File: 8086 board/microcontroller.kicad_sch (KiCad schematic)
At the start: 7 parts, among them U10 74HC595, U11 74HC595, U12 74HC595, U13 74HC165, U14 74HC165, U2 ATmega328P-A, U25 CP2102N-Axx-xQFN28

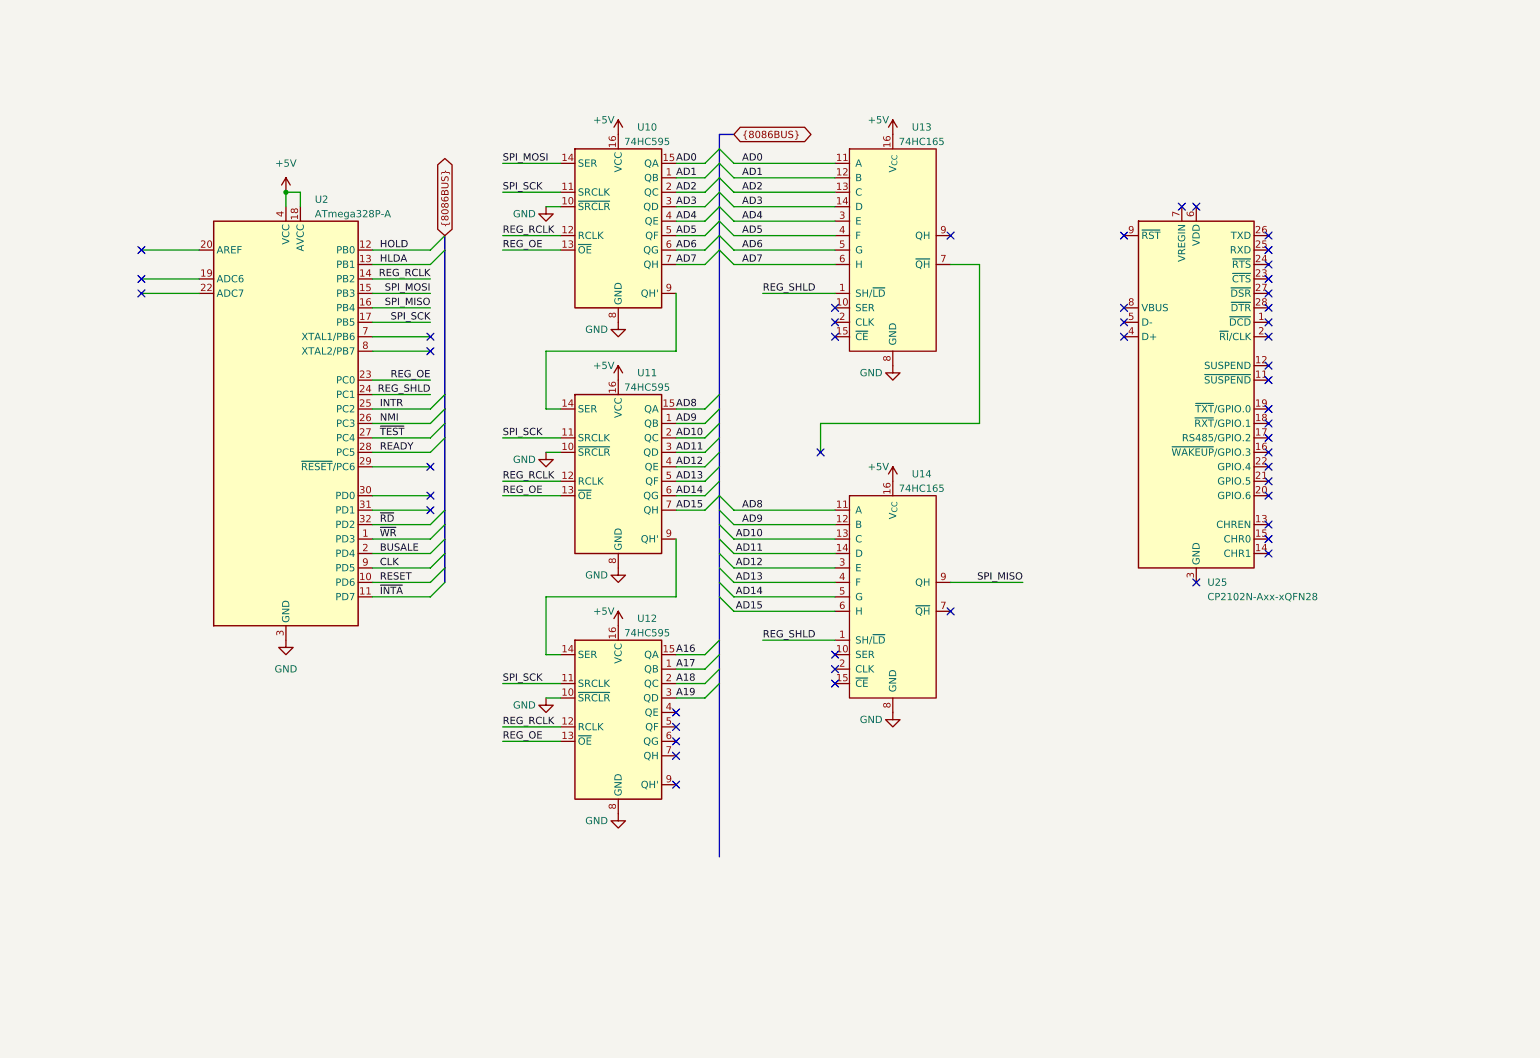
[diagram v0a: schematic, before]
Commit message: refactoring schematic files and structure
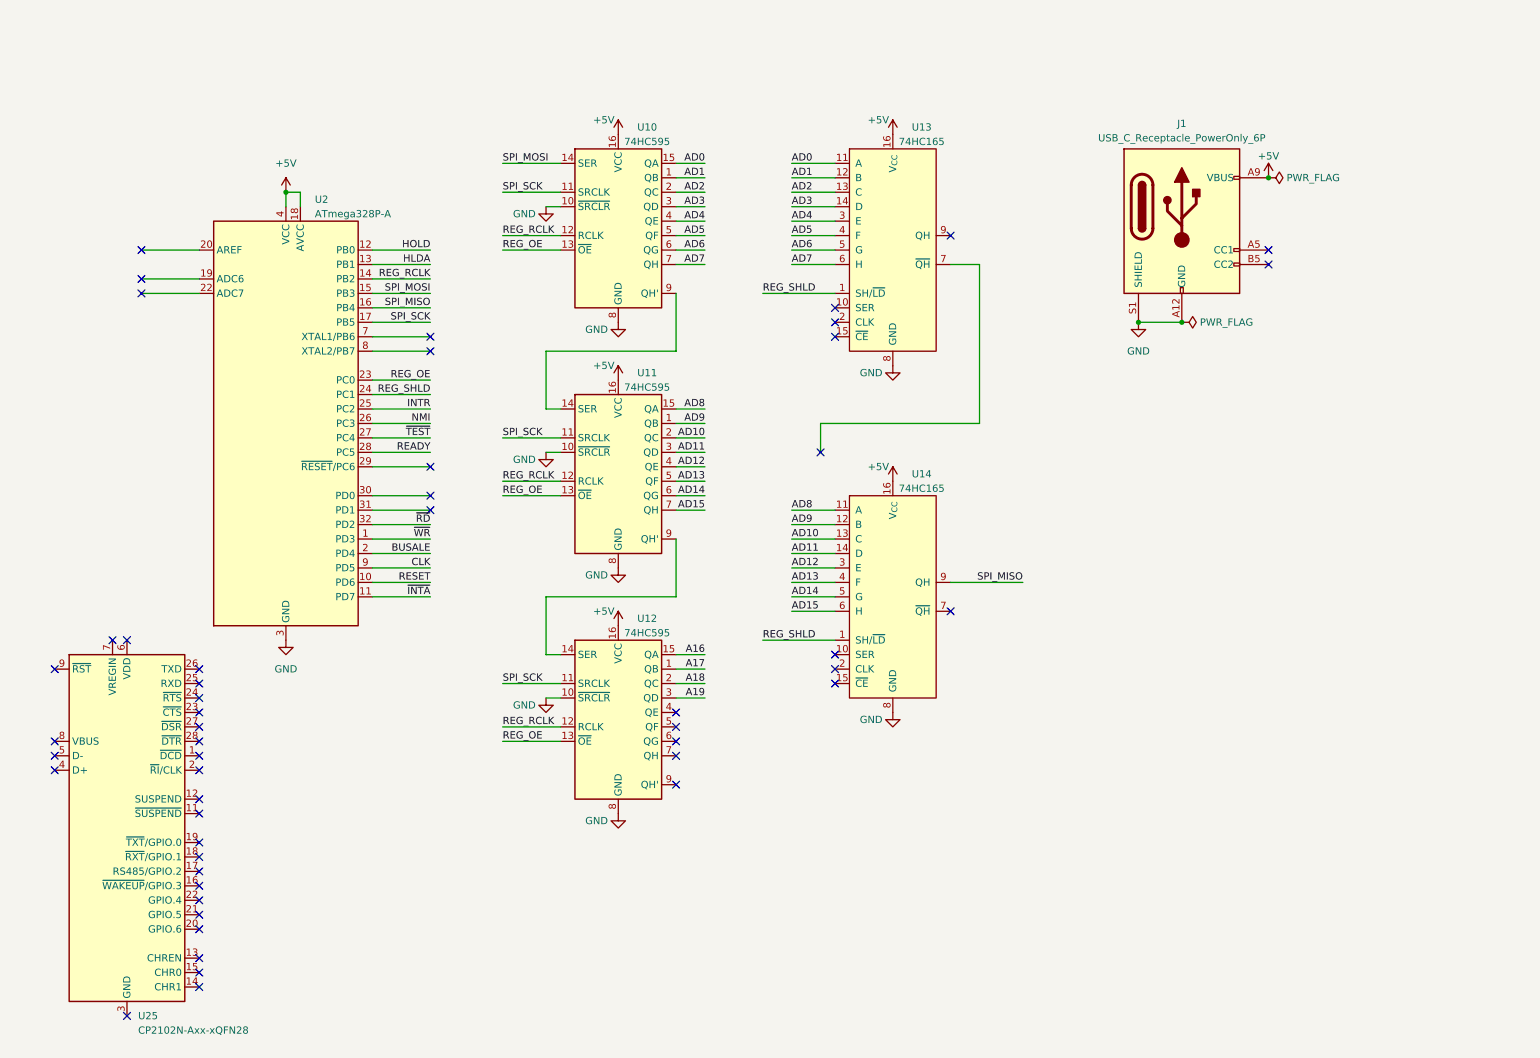
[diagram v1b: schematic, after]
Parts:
- added J1: USB_C_Receptacle_PowerOnly_6P, symbol Connector:USB_C_Receptacle_PowerOnly_6P
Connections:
- net +5V: now also J1.A9 (VBUS), J1.B9 (VBUS)
- net GND: now also J1.A12 (GND), J1.B12 (GND), J1.S1 (SHIELD)
- no-connect marks 49 -> 51
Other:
- moved on the sheet: U25

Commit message: better schematic. initial pcb layout
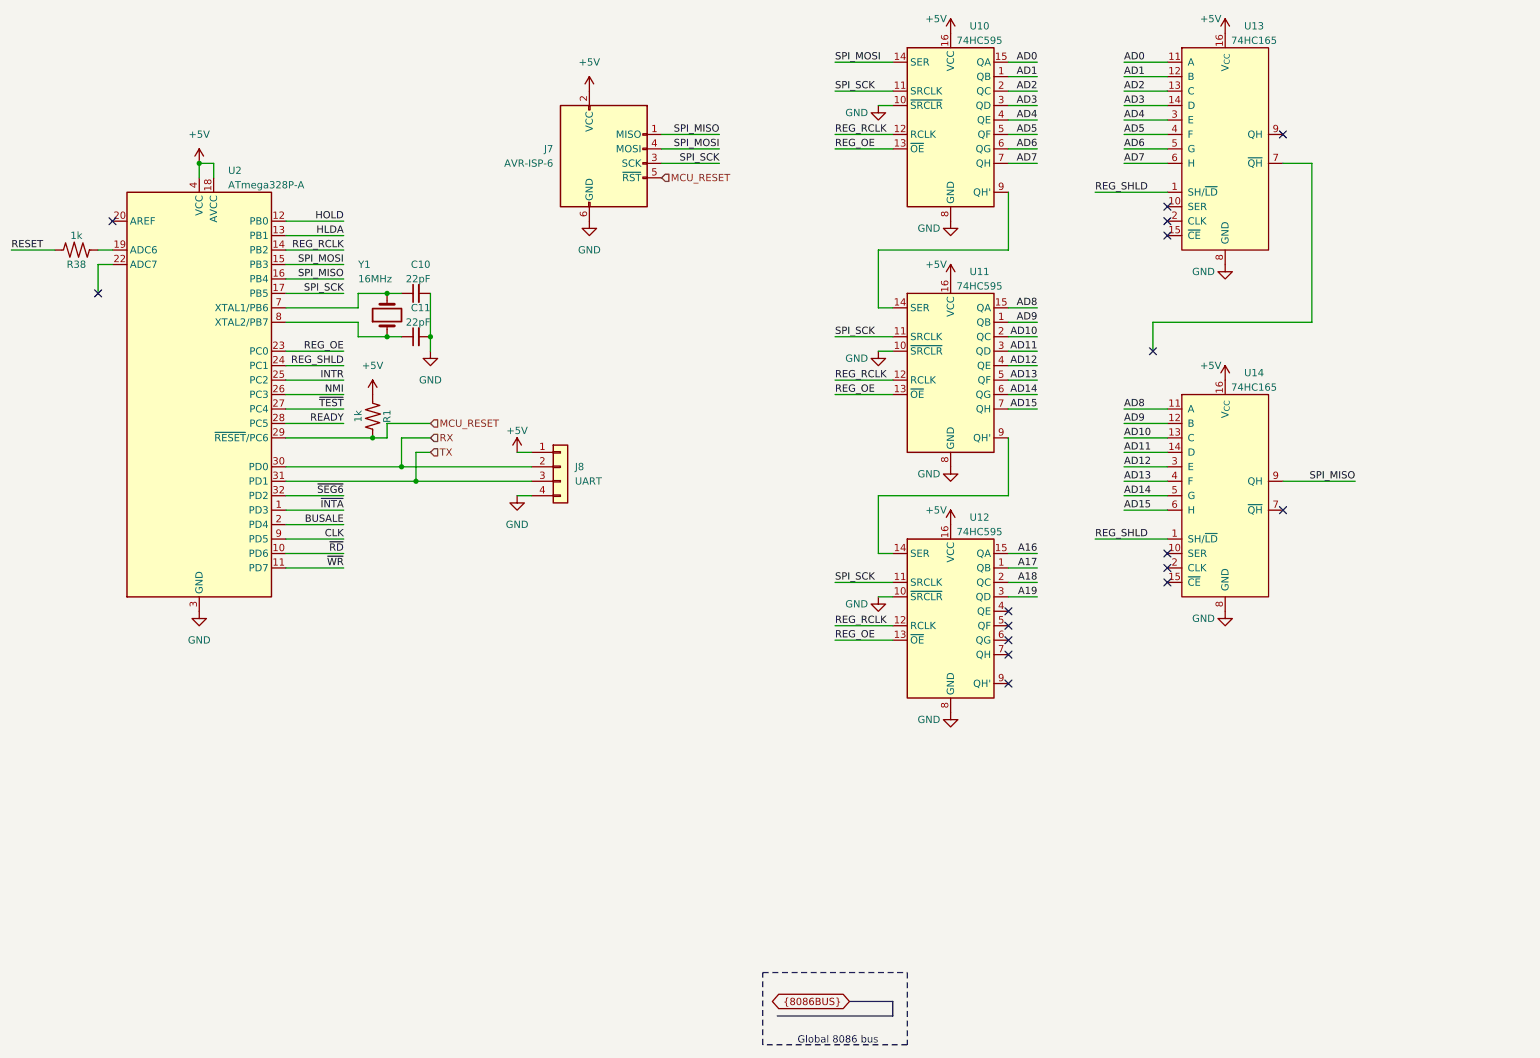
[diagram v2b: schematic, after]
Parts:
- removed J1: USB_C_Receptacle_PowerOnly_6P, symbol Connector:USB_C_Receptacle_PowerOnly_6P
- removed U25: CP2102N-Axx-xQFN28, Package_DFN_QFN:QFN-28-1EP_5x5mm_P0.5mm_EP3.35x3.35mm, symbol Interface_USB:CP2102N-Axx-xQFN28
- added C10, C11: 22pF, symbol Device:C_Small
- added J7: AVR-ISP-6, symbol Connector:AVR-ISP-6
- added J8: UART, symbol Connector_Generic:Conn_01x04
- added R1, R38: 1k, symbol 8086PC:R
- added Y1: 16MHz, symbol Device:Crystal
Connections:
- net +5V: now also J7.2 (VCC), J8.1 (Pin_1), R1.2
- net GND: now also C10.2, C11.2, J7.6 (GND), J8.4 (Pin_4)
- net RESET: now also R38.2; no longer U2.10 (PD6)
- net SPI_MISO: now also J7.1 (MISO)
- net SPI_MOSI: now also J7.4 (MOSI)
- net SPI_SCK: now also J7.3 (SCK)
- net ~{INTA}: now also U2.1 (PD3); no longer U2.11 (PD7)
- net ~{RD}: now also U2.10 (PD6); no longer U2.32 (PD2)
- net ~{WR}: now also U2.11 (PD7); no longer U2.1 (PD3)
- net at U2.19 (ADC6): now also R38.1
- net MCU_RESET: now reaches U2.29 (~{RESET}/PC6)
- net MCU_RESET: now also J7.5 (~{RST}), R1.1
- net RX: now reaches U2.30 (PD0)
- net RX: now also J8.2 (Pin_2)
- net TX: now reaches U2.31 (PD1)
- net TX: now also J8.3 (Pin_3)
- net at U2.7 (XTAL1/PB6): now also C10.1, Y1.2
- net at U2.8 (XTAL2/PB7): now also C11.1, Y1.1
- new net ~{SEG6}: U2.32 (PD2)
- no-connect marks 51 -> 16
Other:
- note added: "Global 8086 bus"
- moved on the sheet: U10, U11, U12, U13, U14, U2

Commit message: Schematic finished! (some footprint assignments are still needed)
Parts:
- removed U10, U11, U12: 74HC595, Package_SO:SOIC-16W_7.5x10.3mm_P1.27mm, symbol 74xx:74HC595
- removed U2: ATmega328P-A, Package_QFP:TQFP-32_7x7mm_P0.8mm, symbol MCU_Microchip_ATmega:ATmega328P-A
- added U30: ATmega328P, Package_QFP:TQFP-32_7x7mm_P0.8mm, symbol 8086PC:ATmega328P
- added U31, U32, U33: 74HC595, Package_SO:SOIC-16_3.9x9.9mm_P1.27mm, symbol 8086PC:74HC595
- J?: renamed from J7; footprint (none) -> Connector_PinHeader_2.54mm:PinHeader_2x03_P2.54mm_Vertical
- J?: renamed from J8; footprint (none) -> Connector_PinHeader_2.54mm:PinHeader_1x04_P2.54mm_Vertical
- R10: renamed from R38; footprint (none) -> Resistor_SMD:R_0603_1608Metric_Pad0.98x0.95mm_HandSolder
- R9: renamed from R1; footprint (none) -> Resistor_SMD:R_0603_1608Metric_Pad0.98x0.95mm_HandSolder
- U34: renamed from U13; footprint Package_SO:SOIC-16W_7.5x10.3mm_P1.27mm -> Package_SO:SOIC-16_3.9x9.9mm_P1.27mm
- U35: renamed from U14; footprint Package_SO:SOIC-16W_7.5x10.3mm_P1.27mm -> Package_SO:SOIC-16_3.9x9.9mm_P1.27mm
- renumbered C11 to C6, C10 to C7
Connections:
- net +5V: now also U30.18 (AV_{CC}), U30.4 (V_{CC}), U30.6 (V_{CC}), U31.10 (~{SRCLR}), U31.16 (V_{CC}), U32.10 (~{SRCLR}), U32.16 (V_{CC}), U33.10 (~{SRCLR}), U33.16 (V_{CC})
- net A16: now also U33.15 (QA)
- net A17: now also U33.1 (QB)
- net A18: now also U33.2 (QC)
- net A19: now also U33.3 (QD)
- net AD0: now also U31.15 (QA)
- net AD1: now also U31.1 (QB)
- net AD10: now also U32.2 (QC)
- net AD11: now also U32.3 (QD)
- net AD12: now also U32.4 (QE)
- net AD13: now also U32.5 (QF)
- net AD14: now also U32.6 (QG)
- net AD15: now also U32.7 (QH)
- net AD2: now also U31.2 (QC)
- net AD3: now also U31.3 (QD)
- net AD4: now also U31.4 (QE)
- net AD5: now also U31.5 (QF)
- net AD6: now also U31.6 (QG)
- net AD7: now also U31.7 (QH)
- net AD8: now also U32.15 (QA)
- net AD9: now also U32.1 (QB)
- net BUSALE: now also U30.1 (PD3[19/1])
- net CLK: now also U30.9 (PD5[21])
- net GND: now also C6.1, C7.1, U34.10 (SER), U34.15 (~{CE}), U35.15 (~{CE}), U30.21 (GND), U30.3 (GND), U30.5 (GND), U31.8 (GND), U32.8 (GND), U33.8 (GND); no longer C6.2, C7.2
- net HLDA: now also U30.24 (PC1[9])
- net HOLD: now also U30.23 (PC0[8])
- net INTR: now also U30.25 (PC2[10])
- net MCU_RESET: now also U30.29 (PC6[14])
- net NMI: now also U30.26 (PC3[11])
- net READY: now also U30.14 (PB2[2])
- net REG_OE: now also U30.13 (PB1[1]), U31.13 (~{OE}), U32.13 (~{OE}), U33.13 (~{OE})
- net RX: now also J?.3 (Pin_3), U30.31 (PD1[17]); no longer J?.2 (Pin_2)
- net SPI_MISO: now also U30.16 (PB4[4])
- net SPI_MOSI: now also U30.15 (PB3[3]), U31.14 (SER)
- net SPI_SCK: now also U34.2 (CLK), U35.2 (CLK), U30.17 (PB5[5]), U31.11 (SRCLK), U32.11 (SRCLK), U33.11 (SRCLK)
- net TX: now also J?.2 (Pin_2), U30.30 (PD0[16]); no longer J?.3 (Pin_3)
- net ~{INTA}: now also U30.27 (PC4[12])
- net ~{RD}: now also U30.10 (PD6[22])
- net ~{SEG6}: now also U30.32 (PD2[18/0])
- net ~{TEST}: now also U30.28 (PC5[13])
- net ~{WR}: now also U30.11 (PD7[23])
- net XTAL1: now reaches Y1.2
- net XTAL1: now also C6.2, U30.7 (PB6[6]); no longer C7.1
- net at U34.9 (QH): now also U35.10 (SER)
- net XTAL2: now reaches Y1.1
- net XTAL2: now also C7.2, U30.8 (PB7[7]); no longer C6.1
- net at R10.1: now also U30.2 (PD4[20])
- net REG_SHLD renamed RCLK_SH/~{LD}
- net RCLK_SH/~{LD}: now also U30.12 (PB0[0]), U31.12 (RCLK), U32.12 (RCLK), U33.12 (RCLK)
- new net: U31.9 (QH'), U32.14 (SER)
- new net: U32.9 (QH'), U33.14 (SER)
- no-connect marks 16 -> 10
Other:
- note added: "ISP"
- note added: "Microcontroller"
- note added: "Shift registers"
- note added: "UART"
- moved on the sheet: C6, C7, J?, R10, R9, U34, U35, Y1

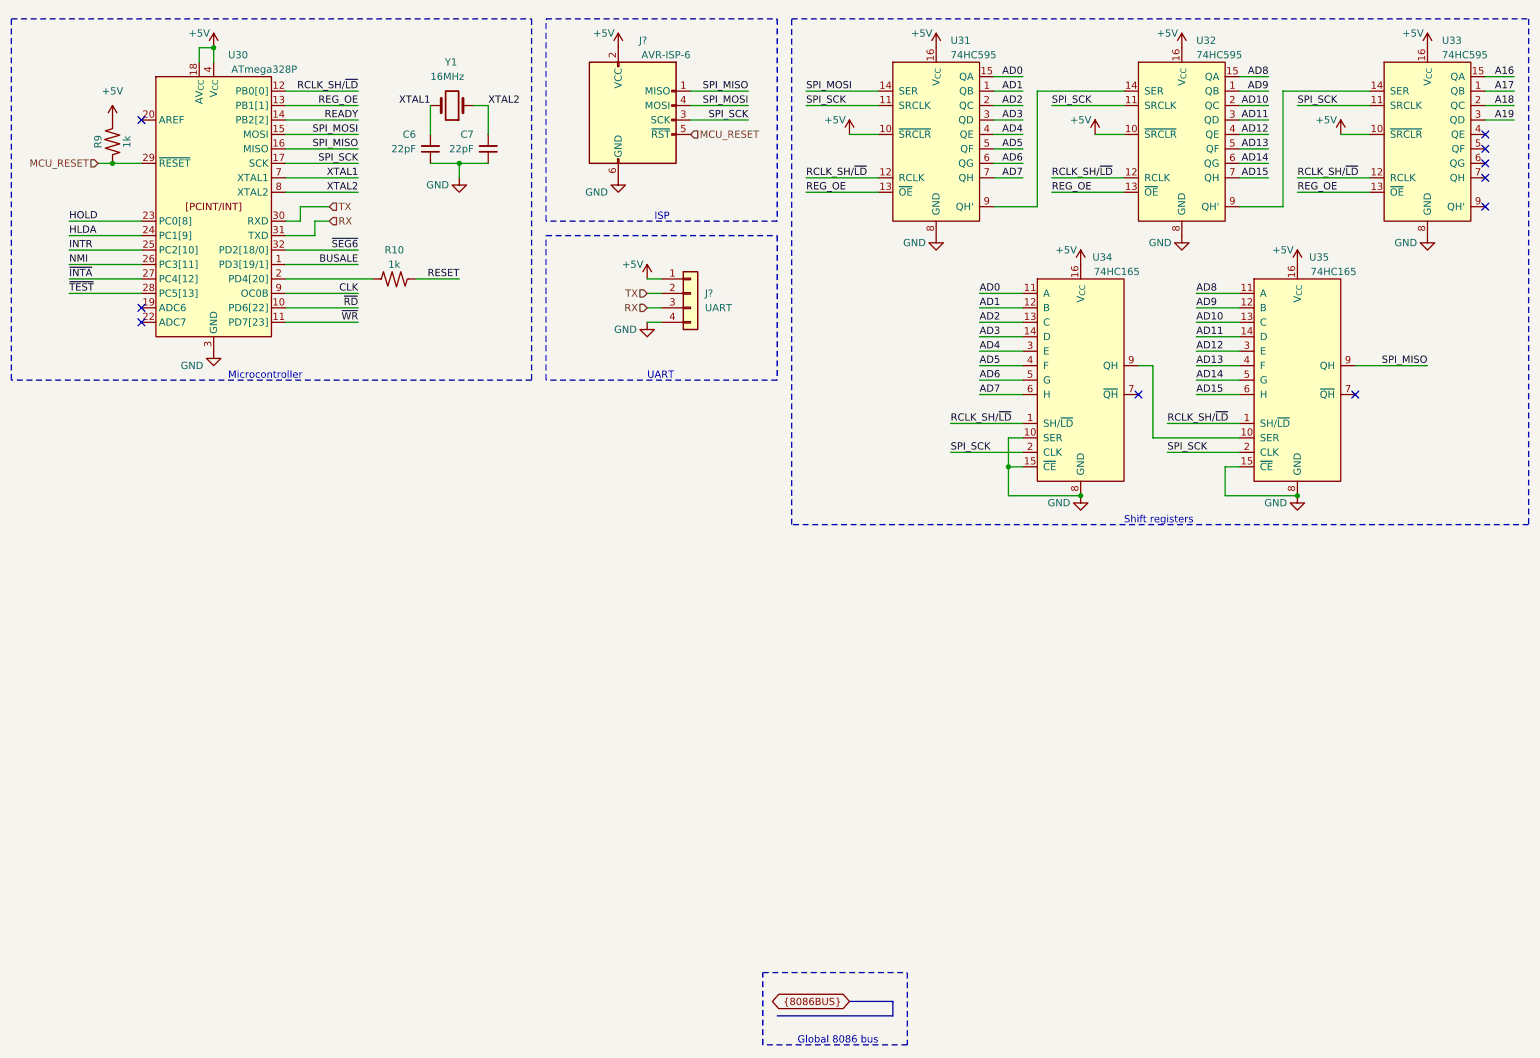
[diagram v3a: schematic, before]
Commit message: change to 4 pin crystal
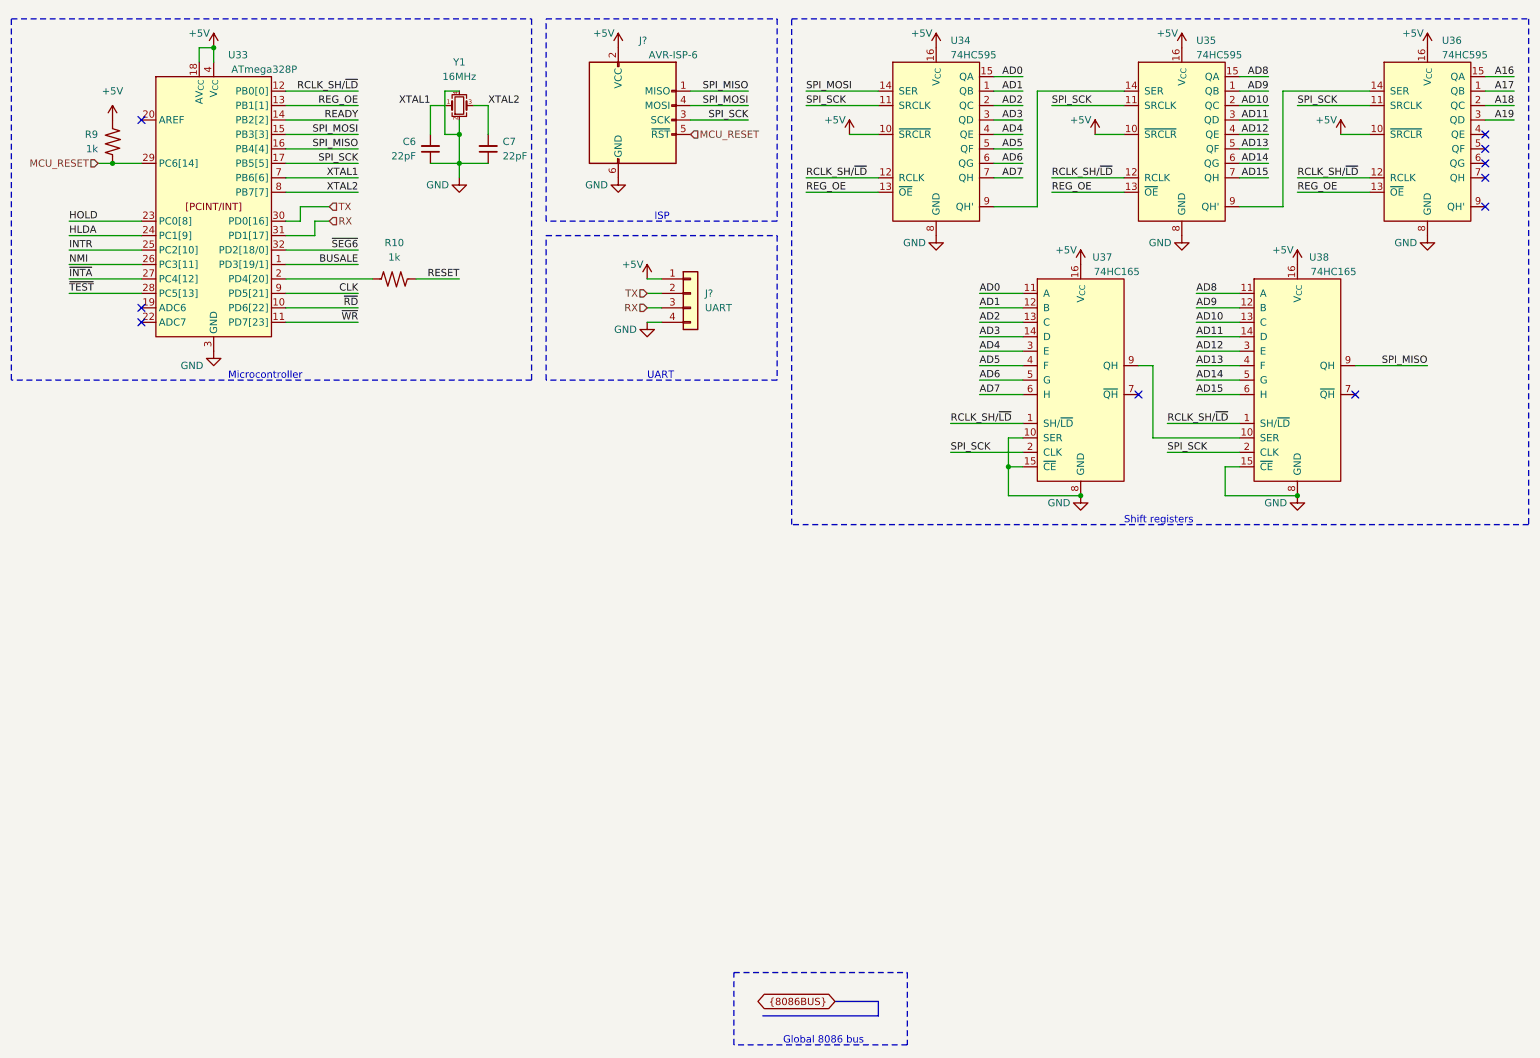
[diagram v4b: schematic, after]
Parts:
- removed Y1: 16MHz, symbol Device:Crystal
- added Y1: 16MHz, Crystal:Crystal_SMD_3225-4Pin_3.2x2.5mm_HandSoldering, symbol Device:Crystal_GND24_Small
- C6, C7: footprint (none) -> Capacitor_SMD:C_0603_1608Metric_Pad1.08x0.95mm_HandSolder
- renumbered U30 to U33, U31 to U34, U32 to U35, U33 to U36, U34 to U37, U35 to U38
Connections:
- net GND: now also Y1.2, Y1.4
- net XTAL1: now also Y1.1
- net XTAL2: now also Y1.3
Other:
- company: (none) -> Eldad Hellerman
- title: (none) -> 8086 computer
- moved on the sheet: C6, R9
